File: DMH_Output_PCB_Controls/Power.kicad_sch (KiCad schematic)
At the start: 76 parts, among them J0 Conn_01x01, J10 Conn_01x06, J100 IDC_02x05, U1 TL072, U10 NE5532, U11 TL074, U12 NE5532, U13 NE5532, U14 NE5532, U15 NE5532, U16 NE5532, U17 NE5532, U18 NE5532, U19 NE5532, U2 LM339, U20 TL072, U21 LM4040LP-10, U24 LM339, U25 LM339, U3 LM339, U4 LM339, U5 LM339, U6 LM339, U7 TL072, U8 TL074, U9 NE5532

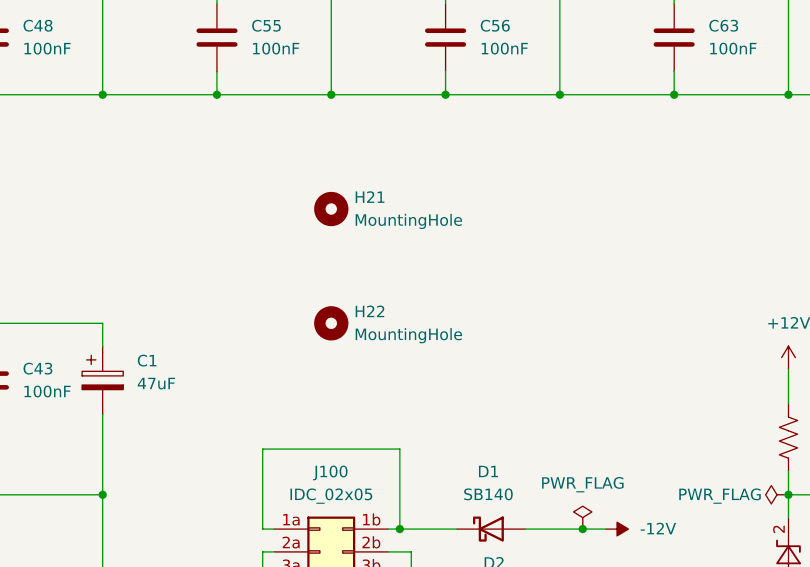
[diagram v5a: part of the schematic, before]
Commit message: Controls PCB placement in progress
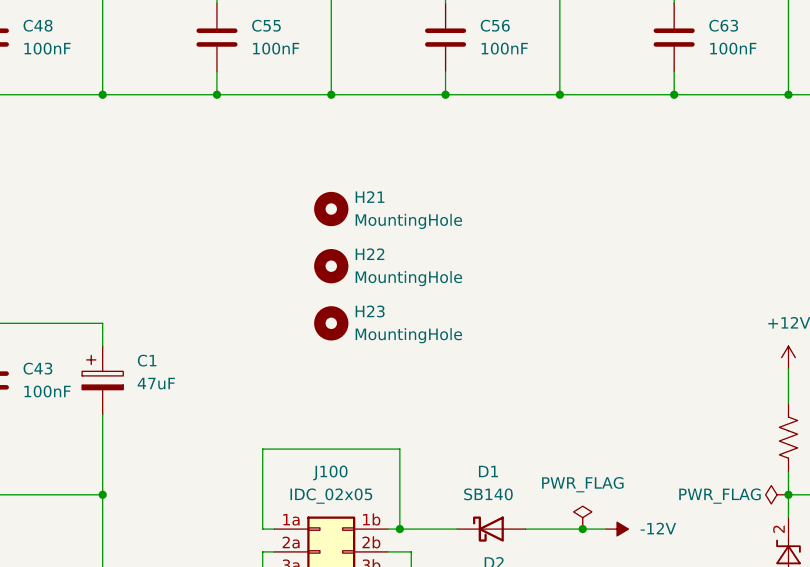
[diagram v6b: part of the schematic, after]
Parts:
- added H23: MountingHole, MountingHole:MountingHole_2.2mm_M2, symbol Mechanical:MountingHole
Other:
- moved on the sheet: H22
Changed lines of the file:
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@@
 	)
 	(symbol
+		(lib_id "Mechanical:MountingHole")
+		(at 101.6 152.4 0)
+		(unit 1)
+		(exclude_from_sim no)
+		(in_bom no)
+		(on_board yes)
+		(dnp no)
+		(fields_autoplaced yes)
+		(property "Reference" "H23"
+			(at 104.14 151.1299 0)
+			(effects
+				(font
+					(size 1.27 1.27)
+				)
+				(justify left)
+			)
+		)
+		(property "Value" "MountingHole"
+			(at 104.14 153.6699 0)
+			(effects
+				(font
+					(size 1.27 1.27)
+				)
+				(justify left)
+			)
+		)
+		(property "Footprint" "MountingHole:MountingHole_2.2mm_M2"
+			(at 101.6 152.4 0)
+			(effects
+				(font
+					(size 1.27 1.27)
+				)
+				(hide yes)
+			)
+		)
+		(property "Datasheet" "~"
+			(at 101.6 152.4 0)
+			(effects
+				(font
+					(size 1.27 1.27)
+				)
+				(hide yes)
+			)
+		)
+		(property "Description" "Mounting Hole without connection"
+			(at 101.6 152.4 0)
+			(effects
+				(font
+					(size 1.27 1.27)
+				)
+				(hide yes)
+			)
+		)
+		(property "Function" ""
+			(at 101.6 152.4 0)
+			(effects
+				(font
+					(size 1.27 1.27)
+				)
+				(hide yes)
+			)
+		)
+		(instances
+			(project "DMH_Output_PCB_Controls"
+				(path "/58f4306d-5387-4983-bb08-41a2313fd315/0cdf34b2-39cd-4d9e-981a-97cd34791509"
+					(reference "H23")
+					(unit 1)
+				)
+			)
+		)
+	)
+	(symbol
 		(lib_id "Device:C")
 		(at 88.9 120.65 0)
@@
 	(symbol
 		(lib_id "Mechanical:MountingHole")
-		(at 101.6 152.4 0)
+		(at 101.6 146.05 0)
 		(unit 1)
 		(exclude_from_sim no)
@@
 		(fields_autoplaced yes)
 		(property "Reference" "H22"
-			(at 104.14 151.1299 0)
+			(at 104.14 144.7799 0)
 			(effects
 				(font
@@
 		)
 		(property "Value" "MountingHole"
-			(at 104.14 153.6699 0)
+			(at 104.14 147.3199 0)
 			(effects
 				(font
@@
 		)
 		(property "Footprint" "MountingHole:MountingHole_2.2mm_M2"
-			(at 101.6 152.4 0)
+			(at 101.6 146.05 0)
 			(effects
 				(font
@@
 		)
 		(property "Datasheet" "~"
-			(at 101.6 152.4 0)
+			(at 101.6 146.05 0)
 			(effects
 				(font
@@
 		)
 		(property "Description" "Mounting Hole without connection"
-			(at 101.6 152.4 0)
+			(at 101.6 146.05 0)
 			(effects
 				(font
@@
 		)
 		(property "Function" ""
-			(at 101.6 152.4 0)
+			(at 101.6 146.05 0)
 			(effects
 				(font
@@
 		(exclude_from_sim no)
 		(in_bom yes)
-		(on_board yes)
+		(on_board no)
 		(dnp no)
 		(fields_autoplaced yes)
@@
 		(exclude_from_sim no)
 		(in_bom yes)
-		(on_board yes)
+		(on_board no)
 		(dnp no)
 		(fields_autoplaced yes)
@@
 		(exclude_from_sim no)
 		(in_bom yes)
-		(on_board yes)
+		(on_board no)
 		(dnp no)
 		(fields_autoplaced yes)
@@
 		(exclude_from_sim no)
 		(in_bom yes)
-		(on_board yes)
+		(on_board no)
 		(dnp no)
 		(fields_autoplaced yes)

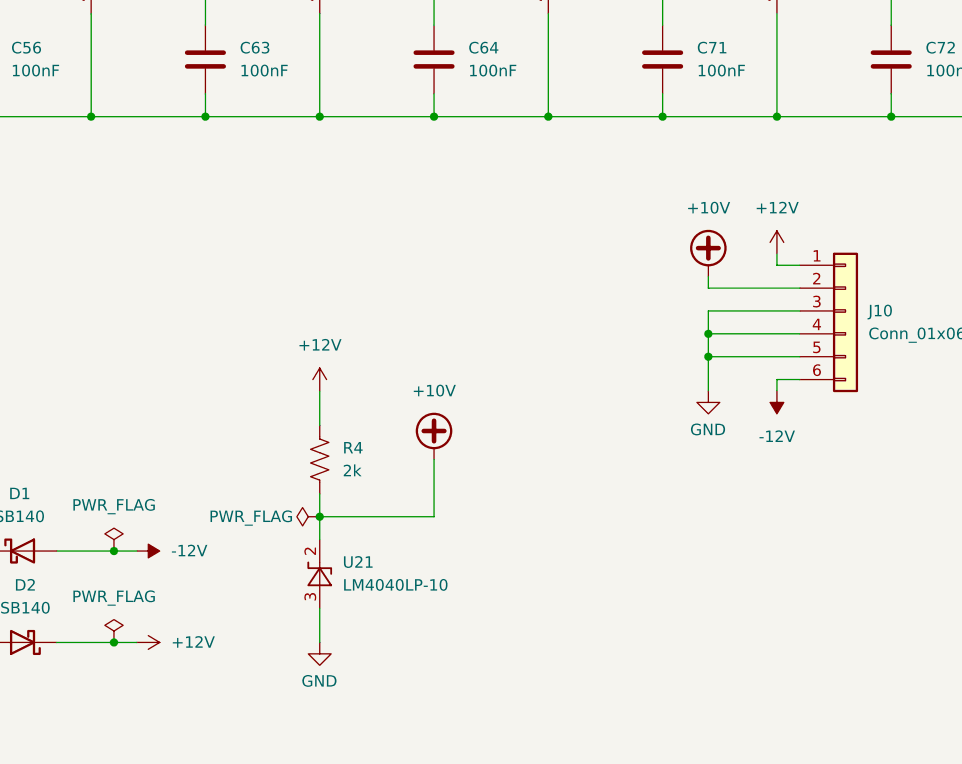
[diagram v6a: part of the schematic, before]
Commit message: Controls PCB comp placement done
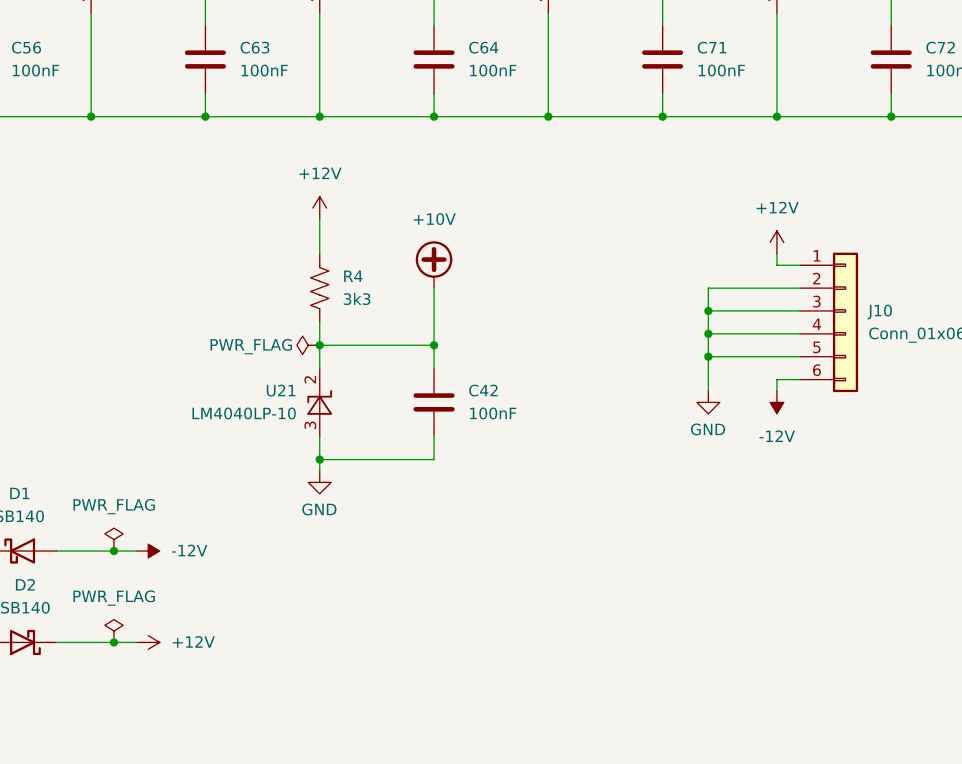
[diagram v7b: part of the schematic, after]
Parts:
- added C42: 100nF, Capacitor_THT:C_Disc_D4.3mm_W1.9mm_P5.00mm, symbol Device:C
- R4: value 2k -> 3k3
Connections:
- net +10V: now also C42.1; no longer J10.2 (Pin_2)
- net GND: now also J10.2 (Pin_2), C42.2
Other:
- moved on the sheet: R4, U21

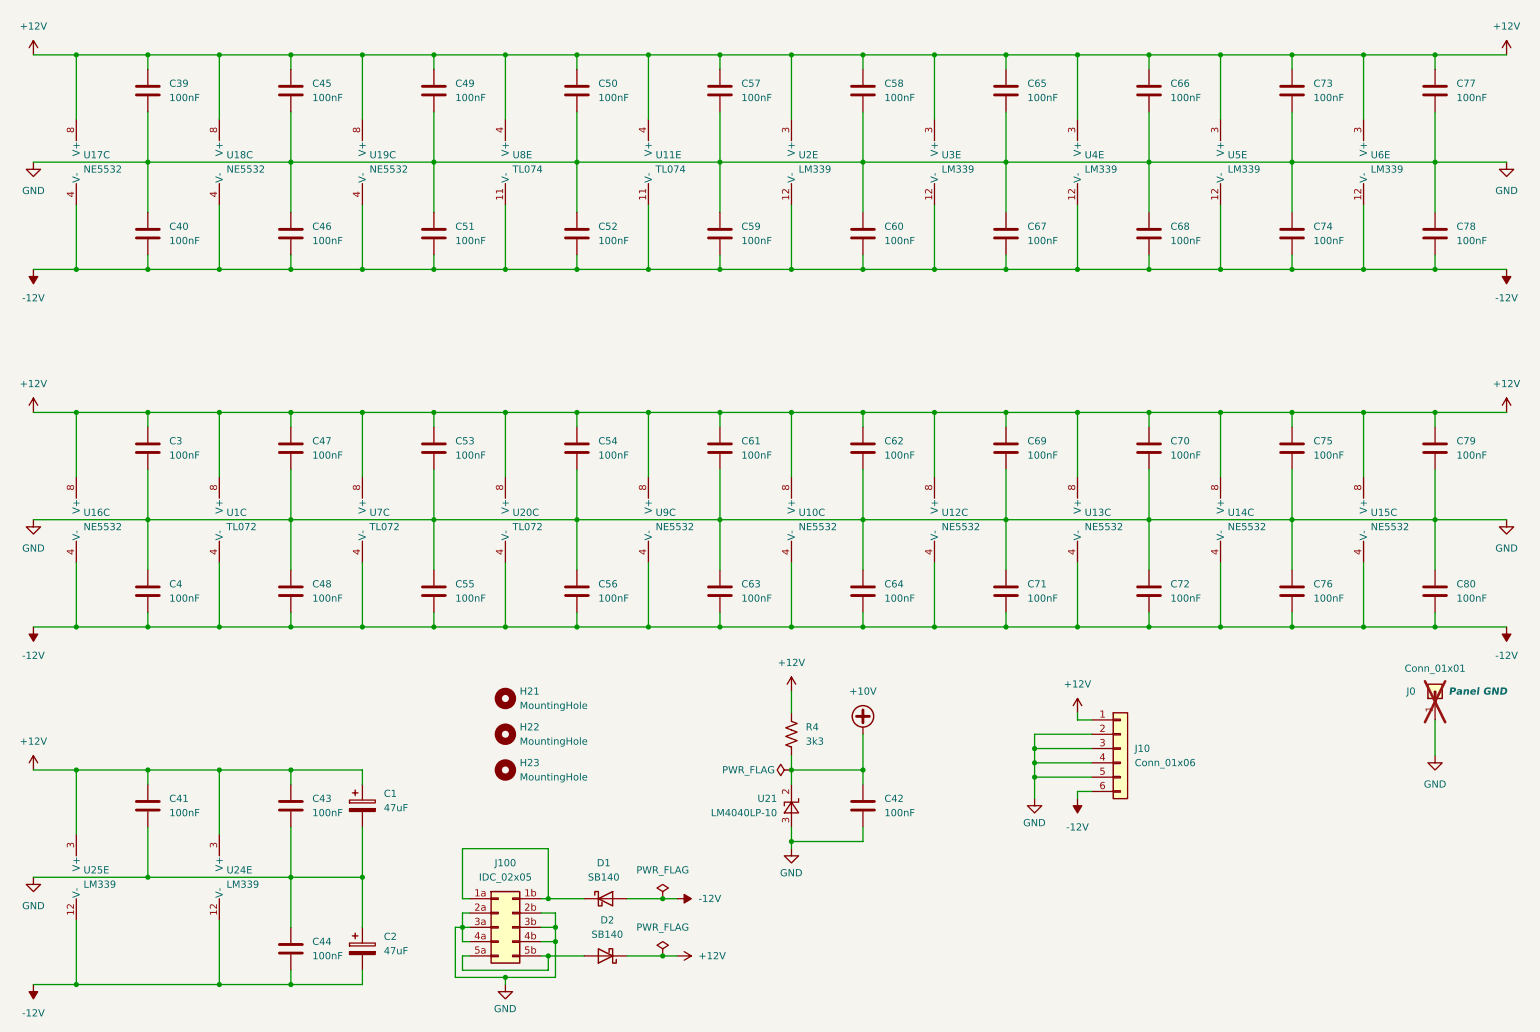
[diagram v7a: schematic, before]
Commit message: Clarifying inter PCB connectors in progress
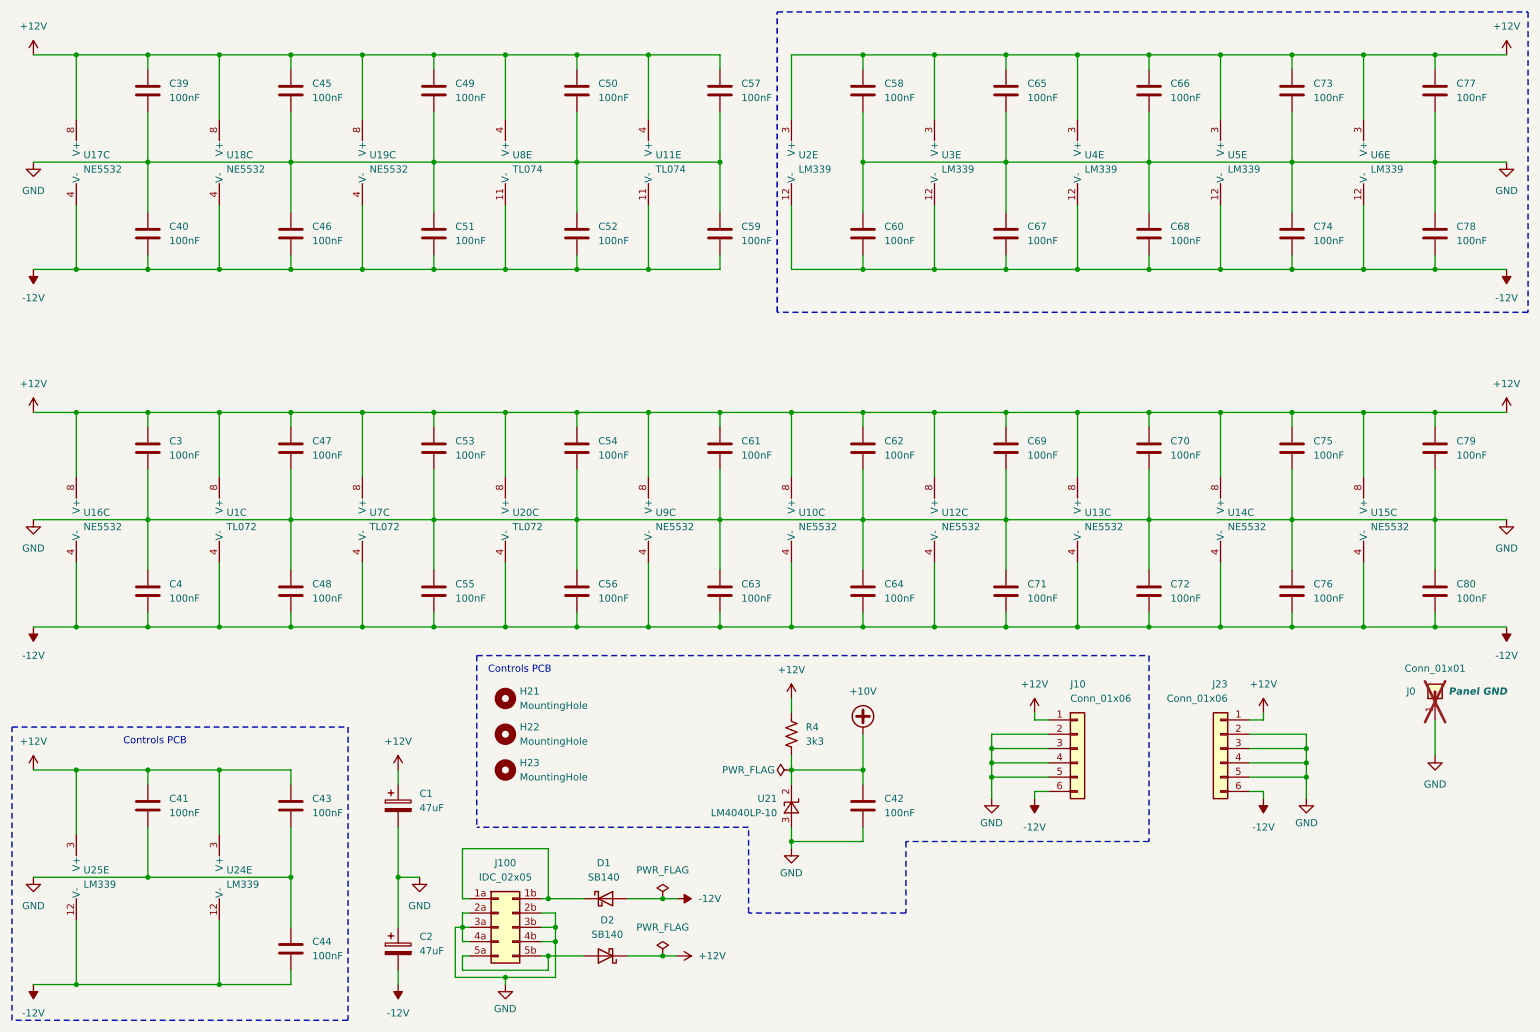
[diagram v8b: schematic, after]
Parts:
- added J23: Conn_01x06, Connector_PinHeader_2.54mm:PinHeader_1x06_P2.54mm_Vertical, symbol Connector_Generic:Conn_01x06
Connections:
- net +12V: now also J23.1 (Pin_1)
- net -12V: now also J23.6 (Pin_6)
- net GND: now also J23.2 (Pin_2), J23.3 (Pin_3), J23.4 (Pin_4), J23.5 (Pin_5)
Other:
- note added: "Controls PCB"
- moved on the sheet: C1, C2, J10
